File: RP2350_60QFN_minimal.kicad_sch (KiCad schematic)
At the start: 43 parts, among them J1 USB_B_Micro, J2 Conn_02x18_Odd_Even, J3 Conn_02x18_Odd_Even, J4 SM03B-SRSS-TB, SW1 SW_Push, SW2 SW_Push, U1 RP2350_60QFN, U2 NCP1117-3.3_SOT223, U3 W25Q128JVS, Y1 ABM8-272-T3

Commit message: update
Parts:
- removed R10: 0, Resistor_SMD:R_0402_1005Metric, symbol Device:R
- removed R9: DNF, Resistor_SMD:R_0402_1005Metric, symbol Device:R
- removed U3: W25Q128JVS, Package_SO:SOIC-8_5.23x5.23mm_P1.27mm, symbol Memory_Flash:W25Q128JVS
- added C20: 10u, Capacitor_SMD:C_0805_2012Metric, symbol Device:C
- added C21, C22: 100n, symbol Device:C
- added U3: BMI270, BMI270:XDCR_BMI270, symbol BMI270:BMI270
- C2: value 100n -> 10u; footprint Capacitor_SMD:C_0402_1005Metric -> Capacitor_SMD:C_0805_2012Metric
- R1: value DNF -> 100k; footprint Resistor_SMD:R_0402_1005Metric -> (none)
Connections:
- net FLASH_SS is gone; now on net GPIO17: R1.2
- net +3V3: now also C20.1
- net GND: now also C20.2, C21.2, C22.2, U3.6 (GNDIO), U3.7 (GND)
- net GPIO15: now also U3.4 (INT1)
- net GPIO16: now also U3.1 (SDO)
- net GPIO17: now also U3.12 (CSB)
- net GPIO18: now also U3.13 (SCX)
- net GPIO19: now also U3.14 (SDX)
- new net: C22.1, U3.5 (VDDIO)
- new net: C21.1, U3.8 (VDD)
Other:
- note removed: "Flash"

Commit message: update
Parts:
- removed C2: 10u, Capacitor_SMD:C_0805_2012Metric, symbol Device:C
- removed J2, J3: Conn_02x18_Odd_Even, Connector_PinHeader_2.54mm:PinHeader_2x18_P2.54mm_Vertical, symbol Connector_Generic:Conn_02x18_Odd_Even
- removed J4: SM03B-SRSS-TB, Connector_JST:JST_SH_SM03B-SRSS-TB_1x03-1MP_P1.00mm_Horizontal, symbol Connector_Generic_MountingPin:Conn_01x03_MountingPin
- removed R4: 1k, Resistor_SMD:R_0402_1005Metric, symbol Device:R
- removed SW2: SW_Push, Button_Switch_SMD:SW_Push_1P1T_NO_Vertical_Wuerth_434133025816, symbol Switch:SW_Push
- added C23: 1u, Capacitor_SMD:C_0805_2012Metric, symbol Device:C
- added J5: Conn_01x07, Connector_PinHeader_2.54mm:PinHeader_1x07_P2.54mm_Vertical, symbol Connector_Generic:Conn_01x07
- added Q1: BSS138, Package_TO_SOT_SMD:SOT-23, symbol Transistor_FET:BSS138
- added R3, R9: 10k, Resistor_SMD:R_0805_2012Metric, symbol Device:R
- added U4: MCP1700T-1802E/TT, Package_TO_SOT_SMD:SOT-23, symbol Regulator_Linear:MCP1700x-180xxTT
- C20: value 10u -> 1u
- C21, C22: footprint (none) -> Capacitor_SMD:C_0805_2012Metric
- R1: footprint (none) -> Resistor_SMD:R_0805_2012Metric
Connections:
- net +3V3: now also C21.1, C22.1, U3.5 (VDDIO), U3.8 (VDD), J5.1 (Pin_1), R9.1, U4.3 (VI)
- net GND: now also C23.2, J5.2 (Pin_2), J5.7 (Pin_7), U4.1 (GND)
- net GPIO14: now also J5.5 (Pin_5)
- net GPIO0 renamed UART_TX
- net UART_TX: now also J5.3 (Pin_3)
- net GPIO1 renamed UART_RX
- net UART_RX: now also J5.4 (Pin_4)
- net GPIO10: no longer names the net of U1.14 (GPIO10)
- net GPIO11: no longer names the net of U1.15 (GPIO11)
- net GPIO12: no longer names the net of U1.16 (GPIO12)
- net GPIO13: no longer names the net of U1.17 (GPIO13)
- net GPIO15 renamed IMU_INT1
- net GPIO16 renamed IMU_MISO
- net GPIO17 renamed IMU_CS
- net GPIO18 renamed IMU_SCK
- net GPIO19 renamed IMU_MOSI
- net GPIO2: no longer names the net of U1.4 (GPIO2)
- net GPIO20: no longer names the net of U1.32 (GPIO20)
- net GPIO21: no longer names the net of U1.33 (GPIO21)
- net GPIO22: no longer names the net of U1.34 (GPIO22)
- net GPIO23: no longer names the net of U1.35 (GPIO23)
- net GPIO24: no longer names the net of U1.36 (GPIO24)
- net GPIO25: no longer names the net of U1.37 (GPIO25)
- net GPIO26_ADC0: no longer names the net of U1.40 (GPIO26_ADC0)
- net GPIO27_ADC1: no longer names the net of U1.41 (GPIO27_ADC1)
- net GPIO28_ADC2: no longer names the net of U1.42 (GPIO28_ADC2)
- net GPIO29_ADC3: no longer names the net of U1.43 (GPIO29_ADC3)
- net GPIO3: no longer names the net of U1.5 (GPIO3)
- net GPIO4: no longer names the net of U1.7 (GPIO4)
- net GPIO5: no longer names the net of U1.8 (GPIO5)
- net GPIO6: no longer names the net of U1.9 (GPIO6)
- net GPIO7: no longer names the net of U1.10 (GPIO7)
- net GPIO8: no longer names the net of U1.12 (GPIO8)
- net GPIO9: no longer names the net of U1.13 (GPIO9)
- net QSPI_SCLK: no longer names the net of U1.56 (QSPI_SCLK)
- net QSPI_SD0: no longer names the net of U1.57 (QSPI_SD0)
- net QSPI_SD1: no longer names the net of U1.59 (QSPI_SD1)
- net QSPI_SD2: no longer names the net of U1.58 (QSPI_SD2)
- net QSPI_SD3: no longer names the net of U1.55 (QSPI_SD3)
- net RUN: no longer names the net of U1.26 (RUN)
- net VBUS: no longer names the net of C1.1, J1.1 (VBUS), U2.3 (VI)
- new net: C23.1, Q1.1 (G), R3.1, U4.2 (VO)
- new net XTR_1V8: J5.6 (Pin_6), Q1.2 (S), R3.2
- new net XTR_3V3: Q1.3 (D), R9.2
- no-connect marks 1 -> 34
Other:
- note removed: "JST Debug Connector"
- moved on the sheet: C19

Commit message: 5v
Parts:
- added D1: PMEG3010ER, Diode_SMD:Nexperia_CFP3_SOD-123W, symbol Diode:PMEG3010ER
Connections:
- net +3V3: no longer C19.1, J5.1 (Pin_1)
- net XTR_3V3: now also U1.17 (GPIO13)
- net at C1.1, J1.1 (VBUS): now also D1.2 (A); no longer U2.3 (VI)
- new net +5V: C19.1, D1.1 (K), J5.1 (Pin_1), U2.3 (VI)
- no-connect marks 34 -> 33
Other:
- moved on the sheet: C5, U2

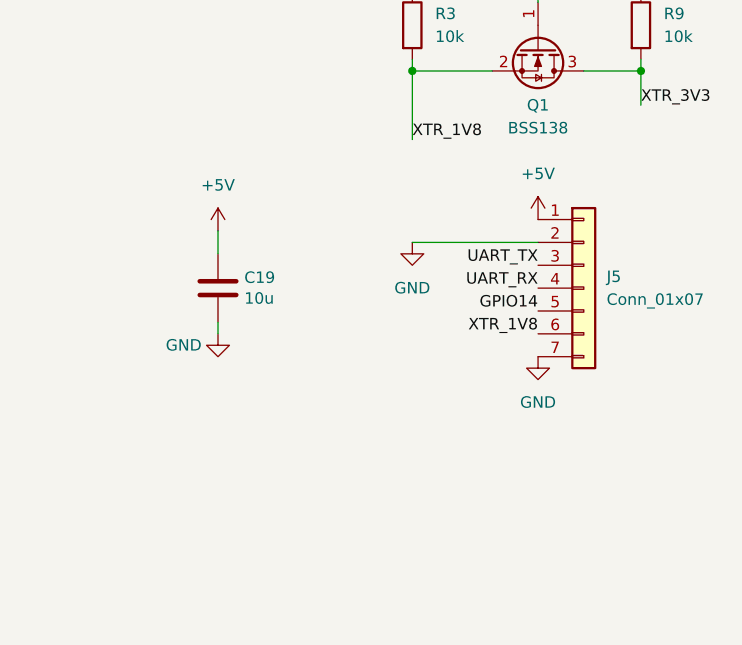
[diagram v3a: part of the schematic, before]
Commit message: try to place components
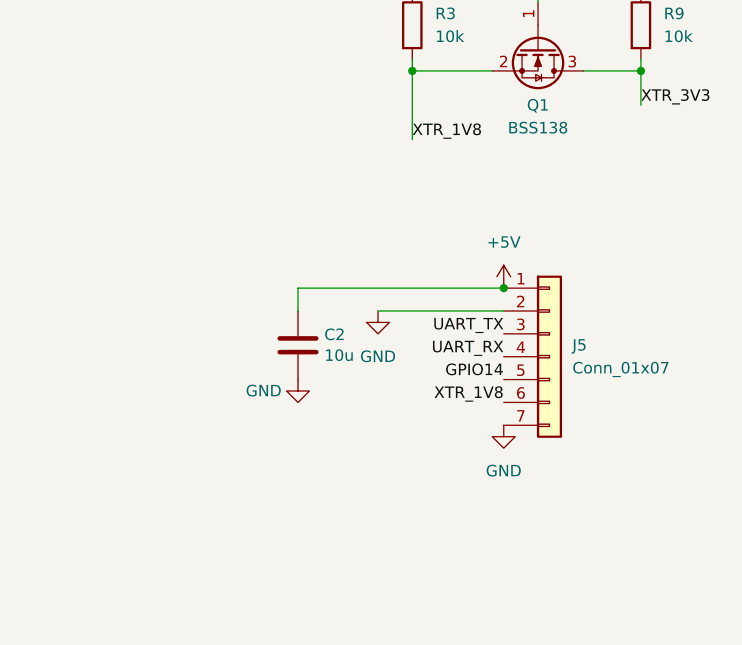
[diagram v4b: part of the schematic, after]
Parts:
- removed C19: 10u, Capacitor_SMD:C_0805_2012Metric, symbol Device:C
- added C2: 10u, Capacitor_SMD:C_0805_2012Metric, symbol Device:C
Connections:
- net +5V: now also C2.1
- net GND: now also C2.2
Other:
- moved on the sheet: J5
